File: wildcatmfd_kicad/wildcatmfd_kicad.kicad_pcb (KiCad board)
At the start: 2 copper layers, 196.9 x 168.9 mm, 29 parts, among them SW1 SW_Push, SW10 SW_Push, SW11 SW_Push, SW12 SW_Push, SW13 SW_Push, SW14 SW_Push, SW15 SW_Push, SW16 SW_Push, SW17 SW_Push, SW18 SW_Push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

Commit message: PCB 2.0
First attempt - 20mm off on screen mount (doh!) - Redesigning PCB to include pass-thru hole for HDMI ribbon cable and adding 3 pin header for +5v for screen power
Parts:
- removed ? (x4), SCREEN_MOUNT (x4): TestPoint_Plated_Hole_D3.0mm, TestPoint:TestPoint_Plated_Hole_D3.0mm
- added J1: MON_PWR, Connector_PinHeader_2.54mm:PinHeader_1x03_P2.54mm_Horizontal, F.Cu at (343.4, 100.2)
- added SCRN_MNT: MountingHole_3mm_Pad, MountingHole:MountingHole_3mm_Pad, F.Cu at (191.0, 28.0)
- added SCRN_MNT: MountingHole_3mm_Pad, MountingHole:MountingHole_3mm_Pad, F.Cu at (191.0, 143.0)
- added SCRN_MNT: MountingHole_3mm_Pad, MountingHole:MountingHole_3mm_Pad, F.Cu at (34.0, 143.0)
- added SCRN_MNT: MountingHole_3mm_Pad, MountingHole:MountingHole_3mm_Pad, F.Cu at (34.0, 28.0)
- moved U1 199.7 mm to (295.0, 14.0)
- moved SW15 187.6 mm to (248.5, 167.9)
- moved SW14 179.6 mm to (268.5, 167.9)
- moved SW13 170.4 mm to (288.5, 167.9)
- moved SW12 162.5 mm to (308.5, 167.9)
- moved SW11 154.6 mm to (328.5, 167.9)
- moved SW20 34.8 mm to (13.5, 22.9)
- moved SW16 24.6 mm to (13.5, 121.9)
- moved SW17 23.4 mm to (13.5, 101.9)
- moved SW18 22.4 mm to (13.5, 81.9)
- moved SW10 21.5 mm to (216.5, 121.9)
- moved SW19 21.4 mm to (13.5, 61.9)
- moved SW9 20.2 mm to (216.5, 101.9)
- moved SW8 18.9 mm to (216.5, 81.9)
- moved SW1 18.1 mm to (54.5, 5.92)
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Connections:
- U1 pad 54: Net-(U1-Pad54) -> +5V
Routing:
- net JOY_05: track 95.8 -> 0.00 mm
- net JOY_16: track 88.6 -> 0.00 mm
- net JOY_04: track 85.3 -> 0.00 mm
- net JOY_01: track 84.9 -> 0.00 mm
- net JOY_20: track 83.1 -> 0.00 mm
- net JOY_15: track 81.7 -> 0.00 mm
- net JOY_14: track 81.7 -> 0.00 mm
- net JOY_17: track 77.1 -> 0.00 mm
- net JOY_11: track 74.9 -> 0.00 mm
- net JOY_03: track 74.8 -> 0.00 mm
- net JOY_02: track 74.4 -> 0.00 mm
- net JOY_18: track 74.1 -> 0.00 mm
- net JOY_10: track 72.1 -> 0.00 mm
- net JOY_06: track 71.7 -> 0.00 mm
- net JOY_19: track 71.6 -> 0.00 mm
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- removed copper zone on B.Cu, net GND
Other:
- board size 196.9 x 168.9 mm -> 225 x 171 mm

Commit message: More PCB work
Finished component positioning
Created board outline
Placed holes for board mounts and screen mounts
SEPTENVIGINTUPLE CHECKED SCREEN MOUNT MEASUREMENTS!
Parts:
- added ?: MountingHole_3mm_Pad, MountingHole:MountingHole_3mm_Pad, F.Cu at (10.0, 161.0)
- added ?: MountingHole_3mm_Pad, MountingHole:MountingHole_3mm_Pad, F.Cu at (215.0, 161.0)
- added ?: MountingHole_3mm_Pad, MountingHole:MountingHole_3mm_Pad, F.Cu at (215.0, 10.0)
- added ?: MountingHole_3mm_Pad, MountingHole:MountingHole_3mm_Pad, F.Cu at (10.0, 10.0)
- moved J1 248.5 mm to (95.0, 108.0)
- moved U1 196.0 mm to (112.5, 85.5)
- moved SW15 191.5 mm to (57.5, 153.9)
- moved SW14 183.0 mm to (86.0, 153.9)
- moved SW13 174.6 mm to (114.5, 153.9)
- moved SW12 166.1 mm to (143.0, 153.9)
- moved SW11 157.6 mm to (171.5, 153.9)
- moved SW20 19.0 mm to (14.5, 41.9)
- moved SW5 4.12 mm to (172.5, 6.92)
- moved SW1 3.64 mm to (58.0, 6.92)
- moved SW2 3.16 mm to (86.5, 6.92)
- moved SW3 2.69 mm to (115.0, 6.92)
- moved SW4 1.12 mm to (144.0, 6.92)
- moved SW10 1.00 mm to (215.5, 121.9)
- moved SW16 1.00 mm to (14.5, 121.9)
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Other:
- outline, holes or cut-outs redrawn
- board text added: "SOLDER TEENSY ON REVERSE"

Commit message: Round 2
Finished new design.
Uploaded to JCLPCB for order.
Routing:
- net JOY_16: track 0.00 -> 100.8 mm
- net JOY_05: track 0.00 -> 95.4 mm
- net JOY_20: track 0.00 -> 94.0 mm
- net JOY_17: track 0.00 -> 90.0 mm
- net JOY_18: track 0.00 -> 86.3 mm
- net JOY_10: track 0.00 -> 85.5 mm
- net JOY_01: track 0.00 -> 84.7 mm
- net JOY_04: track 0.00 -> 84.6 mm
- net JOY_06: track 0.00 -> 84.4 mm
- net JOY_19: track 0.00 -> 83.2 mm
- net JOY_15: track 0.00 -> 82.9 mm
- net JOY_14: track 0.00 -> 82.7 mm
- net JOY_11: track 0.00 -> 76.2 mm
- net JOY_09: track 0.00 -> 74.7 mm
- net JOY_02: track 0.00 -> 73.9 mm
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- added copper zone on B.Cu, net GND
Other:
- outline, holes or cut-outs redrawn
- board text added: "HDMI RIBBON PASSTHRU"
- board text added: "JCLJCLJCLJCL"
- board text added: "MONITOR POWER"
- board text added: "SOLDER TEENSY 3.6 ON REVERSE"
- board text added: "TEENSY 3.6"
- board text added: "WILDCAT MFD v1.0 DESIGNED BY JEREMY KELLOGG"
- board text removed: "SOLDER TEENSY ON REVERSE"

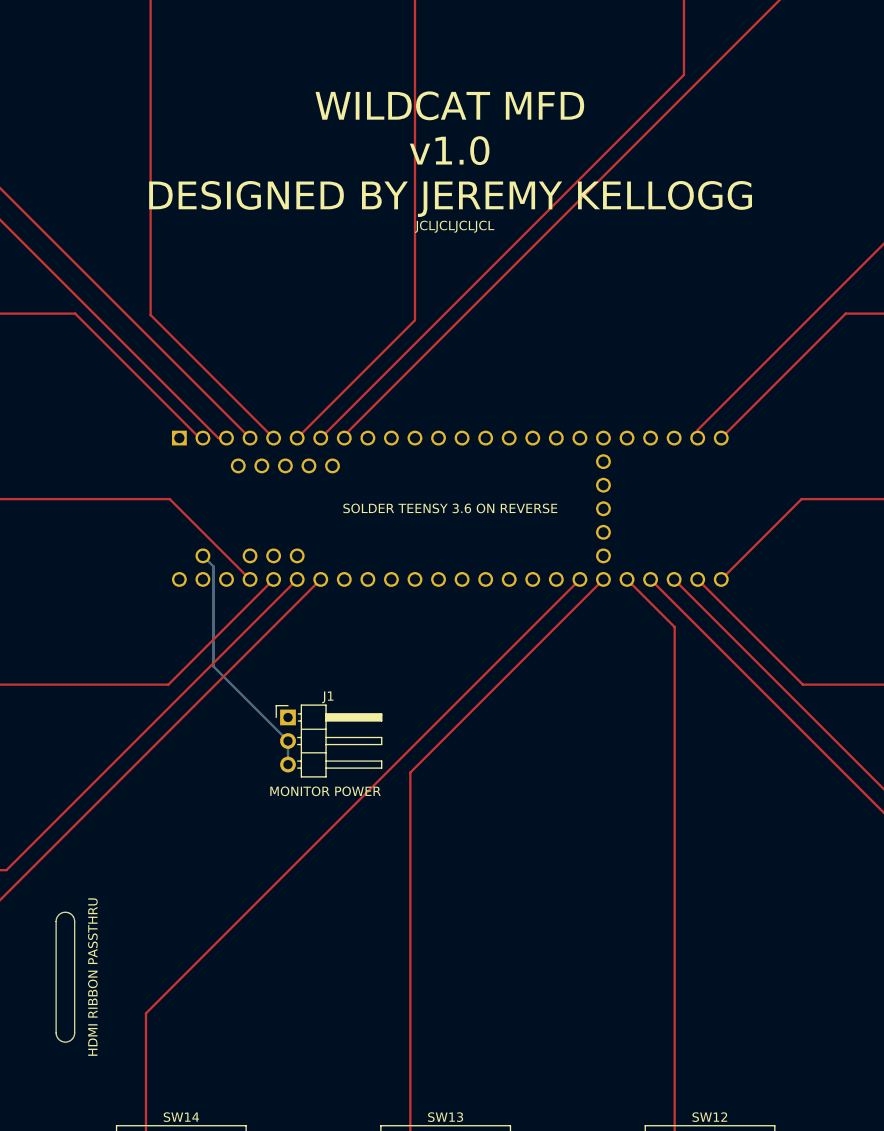
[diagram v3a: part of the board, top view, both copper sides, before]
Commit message: Fixed again
Adjusted location of HDMI cable pass-thru slot
Remembered to turn the damned flood fill for the ground plane back on!
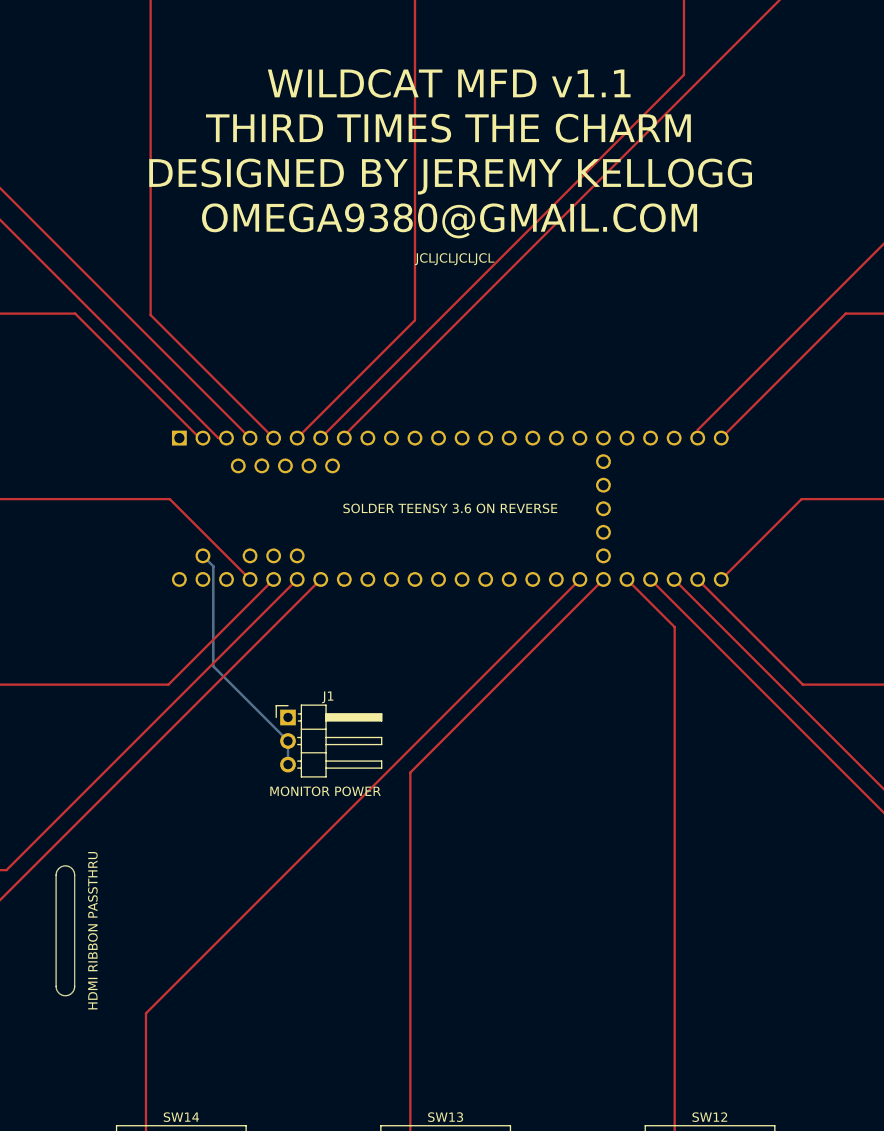
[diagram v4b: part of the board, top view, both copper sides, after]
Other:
- outline, holes or cut-outs redrawn
- board text added: "WILDCAT MFD v1.1 THIRD TIMES THE CHARM DESIGNED BY JEREMY KELLOGG OMEGA9380@GMAIL.COM"
- board text removed: "WILDCAT MFD v1.0 DESIGNED BY JEREMY KELLOGG"
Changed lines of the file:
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@@
-(kicad_pcb (version 20171130) (host pcbnew "(5.1.9)-1")
+(kicad_pcb (version 20171130) (host pcbnew 5.1.5+dfsg1-2build2)
   (general
     (thickness 1.6)
@@
       (drillshape 0)
       (scaleselection 1)
-      (outputdirectory "E:/Documents/GitHub/WildCatMFD/wildcatmfd_gerber/"))
+      (outputdirectory "../wildcatmfd_gerber/"))
   )
   (net 0 "")
@@
     )
   )
-  (gr_text JCLJCLJCLJCL (at 113 55) (layer F.SilkS)
-    (effects (font (size 1 1) (thickness 0.0375)))
-  )
-  (gr_text "WILDCAT MFD\nv1.0\nDESIGNED BY JEREMY KELLOGG" (at 112.5 47) (layer F.SilkS)
-    (effects (font (size 3 3) (thickness 0.15)))
+  (gr_text JCLJCLJCLJCL (at 113 58.5) (layer F.SilkS)
+    (effects (font (size 1 1) (thickness 0.1)))
+  )
+  (gr_text "WILDCAT MFD v1.1\nTHIRD TIMES THE CHARM\nDESIGNED BY JEREMY KELLOGG\nOMEGA9380@GMAIL.COM" (at 112.5 47) (layer F.SilkS)
+    (effects (font (size 3 3) (thickness 0.5)))
   )
   (gr_text "MONITOR POWER" (at 99 116) (layer F.SilkS)
@@
     (effects (font (size 1 1) (thickness 0.15)) (justify mirror))
   )
-  (gr_text "HDMI RIBBON PASSTHRU" (at 74 136 90) (layer F.SilkS)
+  (gr_text "HDMI RIBBON PASSTHRU" (at 74 131 90) (layer F.SilkS)
     (effects (font (size 1 1) (thickness 0.15)))
   )
-  (gr_arc (start 71 142) (end 70 142) (angle -180) (layer Edge.Cuts) (width 0.1))
-  (gr_arc (start 71 130) (end 72 130) (angle -180) (layer Edge.Cuts) (width 0.1))
-  (gr_line (start 72 130) (end 72 142) (layer Edge.Cuts) (width 0.1))
-  (gr_line (start 70 130) (end 70 142) (layer Edge.Cuts) (width 0.1))
+  (gr_arc (start 71 137) (end 70 137) (angle -180) (layer Edge.Cuts) (width 0.1))
+  (gr_arc (start 71 125) (end 72 125) (angle -180) (layer Edge.Cuts) (width 0.1))
+  (gr_line (start 72 125) (end 72 137) (layer Edge.Cuts) (width 0.1))
+  (gr_line (start 70 125) (end 70 137) (layer Edge.Cuts) (width 0.1))
   (gr_text "SOLDER TEENSY 3.6 ON REVERSE" (at 112.5 85.5) (layer F.SilkS)
     (effects (font (size 1 1) (thickness 0.15)))
@@
     (connect_pads (clearance 0.508))
     (min_thickness 0.254)
-    (fill (arc_segments 32) (thermal_gap 0.508) (thermal_bridge_width 0.508))
+    (fill yes (arc_segments 32) (thermal_gap 0.508) (thermal_bridge_width 0.508))
     (polygon
       (pts
